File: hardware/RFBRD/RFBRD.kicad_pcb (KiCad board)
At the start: 2 copper layers, 95 parts, among them J1 SMACONN, J2 SMACONN, P1 CONN_01X08, Q1 Q_NPN_BCE, Q2 Q_NMOS_DGS, Q3 Q_NMOS_DGS, Q4 Q_PMOS_DGS, Q5 Q_PMOS_DGS, Q6 Q_NMOS_DGS, U1 AX5043, U2 AFT05M3S003N, U3 SKY13374

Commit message: Added some Amplification Chain work.
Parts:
- removed 16MHz1: Crystal, Crystals:Crystal_HC49-SD_SMD
- removed 9pF1, 9pF2: C, Capacitors_SMD:C_0805
- removed W8: TEST_1P, Measurement_Points:Test_Point_Keystone_5019_Minature
- added C37: 20pF, Capacitors_SMD:C_0805, F.Cu at (227.6, 47.5)
- added C38: 20pF, Capacitors_SMD:C_0805, F.Cu at (231.6, 47.5)
- added P2: CONN_01X02, Pin_Headers:Pin_Header_Straight_1x02, F.Cu at (213.0, 84.8)
- added Y1: 16MHz, Crystals:Crystal_HC49-SD_SMD, F.Cu at (235.9, 51.8)
- moved L11 340.6 mm to (489.1, 100.4)
- moved C22 336.1 mm to (484.6, 106.9)
- moved L9 332.9 mm to (481.2, 93.9)
- moved L10 330.2 mm to (478.1, 124.2)
- moved L8 322.7 mm to (470.6, 85.8)
- moved C32 321.5 mm to (470.0, 105.0)
- moved C14 321.3 mm to (469.6, 95.2)
- moved Q4 314.9 mm to (461.1, 67.2)
- moved C13 313.7 mm to (461.0, 77.3)
- moved C23 310.3 mm to (458.4, 89.5)
- moved R11 308.8 mm to (457.1, 117.3)
- moved R2 307.6 mm to (454.0, 69.1)
- moved Q6 303.6 mm to (451.5, 124.8)
- moved C31 303.6 mm to (452.0, 96.0)
- moved R1 302.9 mm to (451.4, 110.9)
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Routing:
- net uc_sysclk: track 0.00 -> 29.5 mm
- net 3V3: track 0.00 -> 27.4 mm
- net uc_sel: track 0.00 -> 23.6 mm
- net Net-(C37-Pad2): track 0.00 -> 23.4 mm
- net Net-(C38-Pad2): track 0.00 -> 22.3 mm
- net uc_clk: track 0.00 -> 18.9 mm
- net uc_IRQ: track 0.00 -> 17.9 mm
- net uc_MISO: track 0.00 -> 17.2 mm
- net uc_MOSI: track 0.00 -> 16.8 mm
- net Net-(C25-Pad1): track 0.00 -> 15.0 mm
- net PWRAMP_SEL: track 0.00 -> 14.5 mm
- net Net-(C7-Pad2): track 0.00 -> 13.2 mm
- net Net-(C27-Pad2): track 0.00 -> 13.0 mm, vias 0 -> 2
- net Net-(C6-Pad1): track 0.00 -> 13.0 mm
- net Net-(Q1-Pad3): track 0.00 -> 11.1 mm
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- added copper zone on F.Cu, net GND
- added copper zone on F.Cu, net Net-(C2-Pad1)
- added copper zone on F.Cu, net Net-(C26-Pad1)
- added copper zone on F.Cu, net Net-(C27-Pad1)
- added copper zone on F.Cu, net Net-(C27-Pad2)
- added copper zone on F.Cu, net Net-(C3-Pad1)
- added copper zone on F.Cu, net Net-(C4-Pad1)
- added copper zone on F.Cu, net Net-(C5-Pad1)
- added copper zone on F.Cu, net Net-(C6-Pad1)
- added copper zone on F.Cu, net Net-(C6-Pad2)
- added copper zone on F.Cu, net RF_PREAMP
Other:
- copper layers 2 -> 4

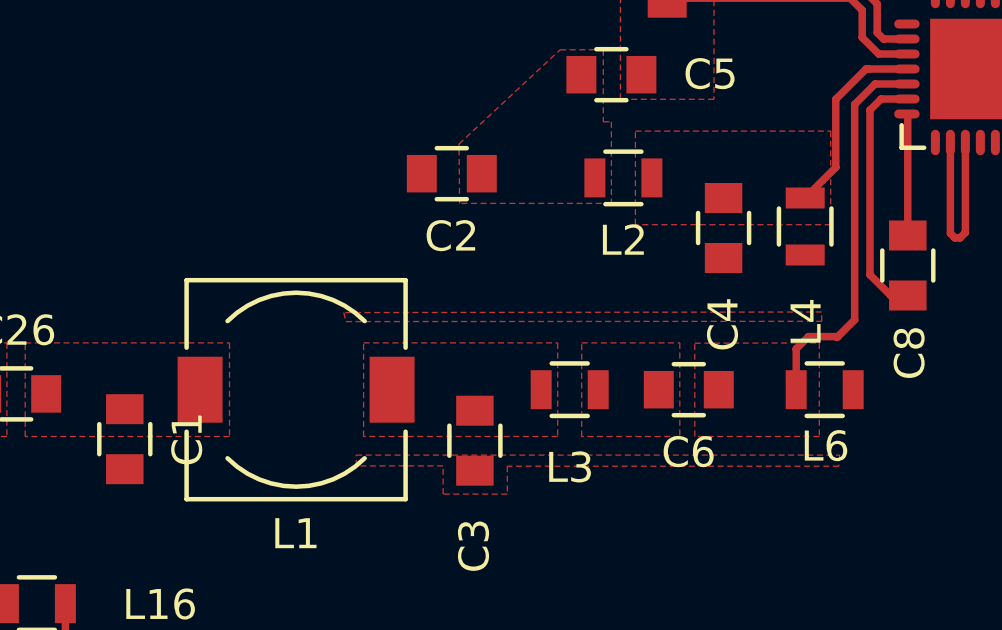
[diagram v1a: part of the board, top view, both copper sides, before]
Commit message: Added some via stitching to start with.
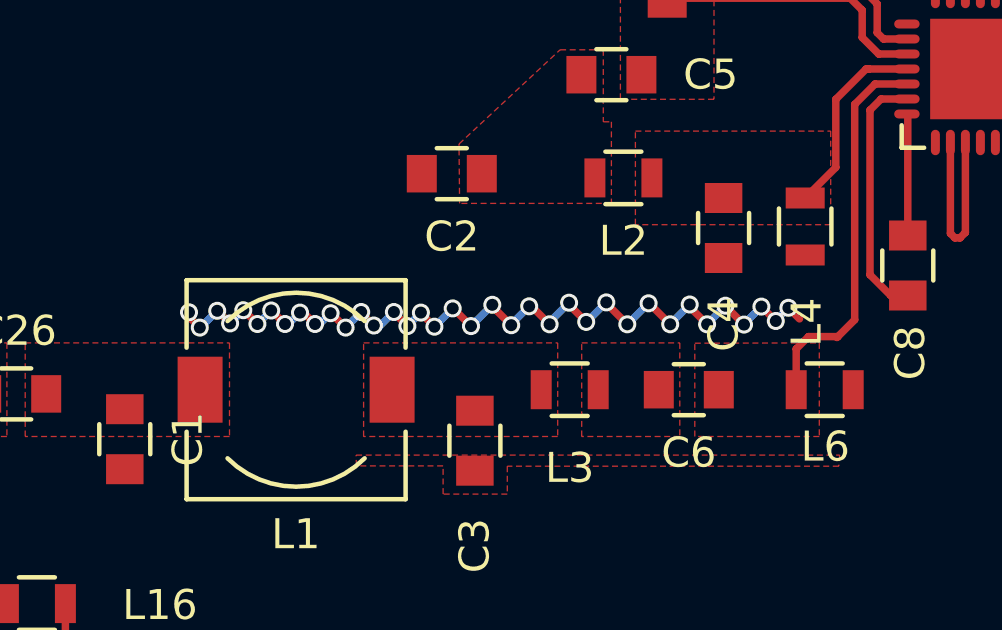
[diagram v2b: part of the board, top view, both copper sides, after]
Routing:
- net (no net): track 0.00 -> 29.3 mm, vias 0 -> 37

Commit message: Added a little more.
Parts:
- moved L10 332.0 mm to (150.0, 73.6)
- moved L8 311.5 mm to (159.4, 73.6)
- moved C13 306.3 mm to (154.7, 75.4), turned to 270 degrees
- moved R2 304.4 mm to (149.8, 79.7)
- moved R1 299.4 mm to (153.6, 79.7)
- moved C15 252.8 mm to (145.3, 75.5), turned to 270 degrees
- moved R3 245.8 mm to (140.6, 73.6)
- moved C11 51.6 mm to (164.1, 75.3), turned to 270 degrees
- moved C10 2.37 mm to (168.8, 73.7)
- moved C29 1.94 mm to (173.2, 75.3)
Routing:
- net (no net): track 29.3 -> 0.00 mm, vias 37 -> 0
- net VBIAS_PWR: track 0.00 -> 6.10 mm
- net Net-(R1-Pad1): track 0.00 -> 2.30 mm
- added copper zone on F.Cu, net Net-(C10-Pad1)
- added copper zone on F.Cu, net Net-(C13-Pad1)
- added copper zone on F.Cu, net PREAMP_TX
- added copper zone on F.Cu, net VBIAS_PWR

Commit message: Added Internals of Board.
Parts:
- moved Q6 386.6 mm to (71.3, 54.7)
- moved Q4 385.7 mm to (75.5, 60.3)
- moved C22 379.4 mm to (106.7, 73.6)
- moved Q3 377.5 mm to (71.3, 60.3)
- moved C32 371.6 mm to (102.8, 48.4), turned to 180 degrees
- moved L11 358.9 mm to (131.1, 75.2), turned to 270 degrees
- moved C31 356.4 mm to (99.0, 46.6), turned to 90 degrees
- moved C23 355.2 mm to (103.5, 75.4), turned to 270 degrees
- moved C30 351.2 mm to (82.8, 57.7), turned to 180 degrees
- moved R10 350.5 mm to (106.0, 46.8), turned to 90 degrees
- moved R11 348.1 mm to (116.2, 46.8), turned to 270 degrees
- moved Q5 339.3 mm to (75.4, 54.7)
- moved C33 329.7 mm to (119.7, 48.4), turned to 180 degrees
- moved L9 320.4 mm to (161.0, 82.2)
- moved R9 317.1 mm to (108.5, 46.8), turned to 270 degrees
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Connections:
- C2 pad 2: RF_IN -> RX_IN
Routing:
- net RX_SWITCH: track 0.00 -> 37.6 mm
- net PWRAMP_SEL: track 14.5 -> 33.0 mm
- net TX_SWITCH: track 0.00 -> 18.0 mm
- net RX_ANT: track 0.00 -> 13.2 mm
- net TX_PASS: track 0.00 -> 12.3 mm
- net PREAMP_TX: track 0.00 -> 12.1 mm
- net AMP_PWR_HV: track 0.00 -> 10.8 mm
- net Net-(R11-Pad1): track 0.00 -> 9.99 mm
- net Net-(J2-Pad1): track 0.00 -> 9.60 mm
- net Net-(C12-Pad1): track 0.00 -> 6.20 mm
- net Net-(C14-Pad1): track 0.00 -> 5.50 mm
- net Net-(L7-Pad2): track 0.00 -> 3.51 mm
- net Net-(Q2-Pad3): track 0.00 -> 3.05 mm
- net VBIAS_PWR: track 6.10 -> 8.60 mm
- added copper zone on F.Cu, net Net-(C19-Pad1)
- added copper zone on F.Cu, net Net-(C20-Pad1)
- added copper zone on F.Cu, net Net-(C21-Pad1)
- added copper zone on F.Cu, net Net-(C31-Pad1)
- added copper zone on F.Cu, net Net-(C32-Pad1)
- added copper zone on F.Cu, net Net-(C33-Pad2)
- added copper zone on F.Cu, net Net-(L11-Pad1)
- added copper zone on F.Cu, net Net-(R3-Pad1)
- added copper zone on F.Cu, net RX_ANT
- added copper zone on F.Cu, net RX_IN
- added copper zone on F.Cu, net TX_OUT
- added copper zone on F.Cu, net TX_PASS
